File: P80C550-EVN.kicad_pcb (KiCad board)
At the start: 4 copper layers, 98 x 68.8 mm, 78 parts, among them J1 VIN, J10 Analog: +5V, J11 Analog: GND, J2 Signals, J3 Address Low, J4 Address High, J5 LCD, J6 UART, J7 UART, J8 I2C, J9 Analog: In, Q1 Si2393DS, SW1 Reset, U1 P80C550EBAA, U10 MAX691xWE, U11 AP62150WU, U12 74VHC1G02, U13 74VHC1G02, U14 74VHC1G02, U15 74LVC1G373, U16 74VHC1G126, U17 74LVC1G07, U18 74LVC1G06, U2 74AC573, U3 HM62256BLP, U4 28C256, U5 MC146818, U6 AM85C30, U7 74AHC138, U8 PCF8584, U9 74AC00, X1 11.0592 MHz, X2 32.768 KHz

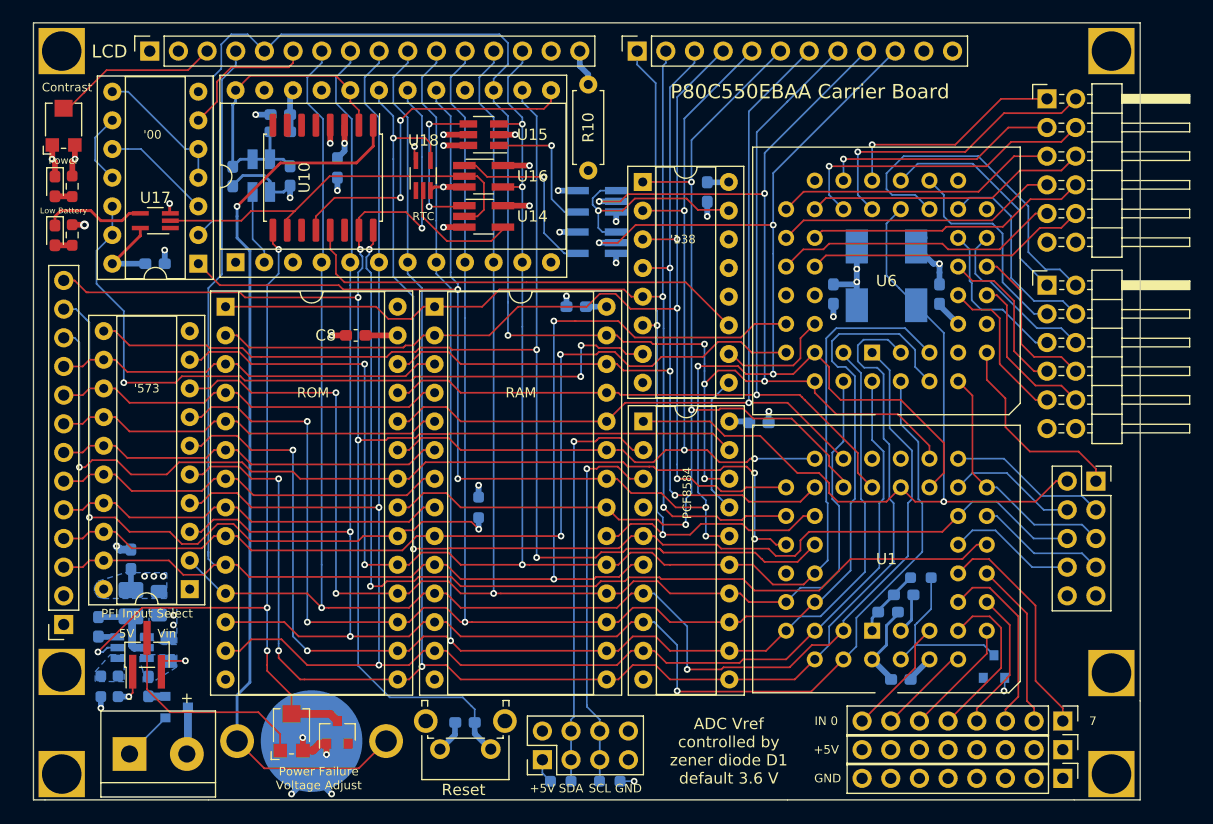
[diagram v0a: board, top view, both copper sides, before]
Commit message: update to KiCAD 6.x and fix the non-inverted reset signal by adding a P-Channel MOSFET to invert the inverted reset signal
Fixes #1 and #2.
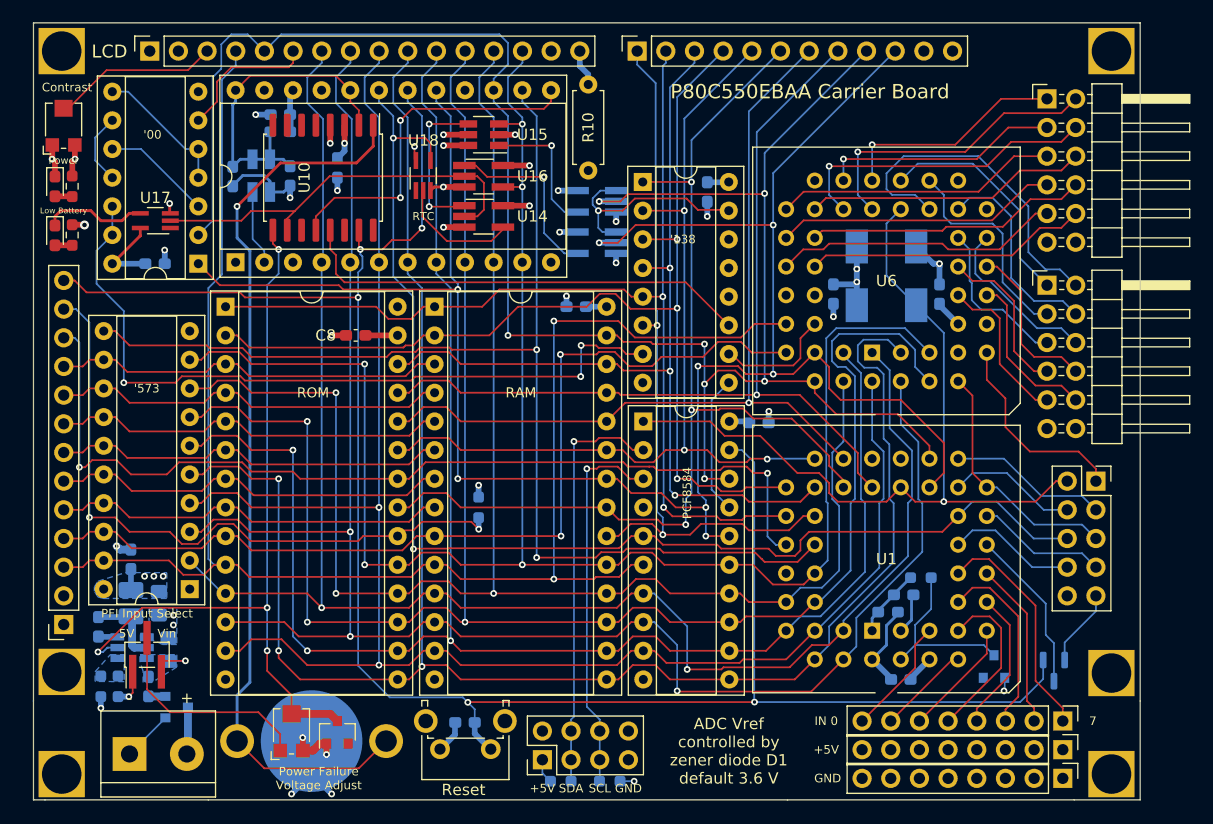
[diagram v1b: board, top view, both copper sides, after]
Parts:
- added Q2: BSS84, Package_TO_SOT_SMD:SOT-23, B.Cu at (188.8, 130.7)
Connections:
- net /~CTSA renamed /~{CTSA}
- net /~CTSB renamed /~{CTSB}
- net /~DCDA renamed /~{DCDA}
- net /~DCDB renamed /~{DCDB}
- net /~DTRA renamed /~{DTRA}
- net /~DTRB renamed /~{DTRB}
- net /~REQA renamed /~{REQA}
- net /~REQB renamed /~{REQB}
- net /~RTSA renamed /~{RTSA}
- net /~RTSB renamed /~{RTSB}
- net /~RTxCA renamed /~{RTxCA}
- net /~RTxCB renamed /~{RTxCB}
- net /~SYNCA renamed /~{SYNCA}
- net /~SYNCB renamed /~{SYNCB}
- net /~TRxCA renamed /~{TRxCA}
- net /~TRxCB renamed /~{TRxCB}
- net ~CODE_CS renamed ~{CODE_CS}
- net ~CODE_RD renamed ~{CODE_RD}
- net ~I2C_CS renamed ~{I2C_CS}
- net ~INT0 renamed ~{INT0}
- net ~INT1 renamed ~{INT1}
- net ~LCD_CS renamed ~{LCD_CS}
- net ~PFO renamed ~{PFO}
- net ~PFO_CS renamed ~{PFO_CS}
- net ~RD renamed ~{RD}
- net ~RST renamed ~{RST}
- net ~RTC_CS renamed ~{RTC_CS}
- net ~RTC_CS_OUT renamed ~{RTC_CS_OUT}
- net ~SCC1_CS renamed ~{SCC1_CS}
- net ~WR renamed ~{WR}
- U1 pad 22: Net-(U1-Pad22) -> unconnected-(U1-Pad22)
- U10 pad 11: Net-(U10-Pad11) -> unconnected-(U10-Pad11)
- U10 pad 14: Net-(U10-Pad14) -> unconnected-(U10-Pad14)
- U10 pad 16: RST -> unconnected-(U10-Pad16)
- U10 pad 5: Net-(U10-Pad5) -> unconnected-(U10-Pad5)
- U10 pad 6: Net-(U10-Pad6) -> unconnected-(U10-Pad6)
- U10 pad 7: Net-(U10-Pad7) -> unconnected-(U10-Pad7)
- U10 pad 8: Net-(U10-Pad8) -> unconnected-(U10-Pad8)
- U5 pad 21: Net-(U5-Pad21) -> unconnected-(U5-Pad21)
- U5 pad 23: Net-(U5-Pad23) -> unconnected-(U5-Pad23)
- U5 pad 3: Net-(U5-Pad3) -> unconnected-(U5-Pad3)
- U7 pad 12: Net-(U7-Pad12) -> unconnected-(U7-Pad12)
- U7 pad 13: Net-(U7-Pad13) -> unconnected-(U7-Pad13)
- U7 pad 14: Net-(U7-Pad14) -> unconnected-(U7-Pad14)
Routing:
- net RST: track 89.8 -> 14.6 mm, vias 2 -> 0
- net ~{RST}: track 135.7 -> 178.1 mm, vias 4 -> 5
- net GND: track 70.1 -> 64.8 mm
- net +5V: track 61.1 -> 66.2 mm
- net /Raw: track 5.23 -> 4.06 mm
- net CLK: track 72.5 -> 71.4 mm
- net /D0: track 147.4 -> 146.3 mm
- net /D5: track 166.8 -> 165.7 mm
- net +15V: track 4.59 -> 3.56 mm
- net /D4: track 157.4 -> 156.5 mm
- net Net-(C16-Pad2): track 4.17 -> 3.38 mm
- net ~{CODE_CS}: track 58.9 -> 58.2 mm
- net /D1: track 159.8 -> 159.2 mm
- net /ADC1: track 8.23 -> 7.72 mm
- net ~{CODE_RD}: track 84.4 -> 84.2 mm, vias 3 -> 2
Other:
- net class Default removed
- board text added: "R/~{W}"
- board text added: "~{CS}"
- board text added: "~{CTS}"
- board text added: "~{DCD}"
- board text added: "~{DTR}"
- board text added: "~{INT0}"
- board text added: "~{INT1}"
- board text added: "~{RD}"
- board text added: "~{REQ}"
- board text added: "~{RST}"
- board text added: "~{RTS}"
- board text added: "~{RTxC}"
- board text added: "~{SYNC}"
- board text added: "~{TRxC}"
- board text added: "~{WR}"
- board text removed: "R/~W"
- board text removed: "~CS"
- board text removed: "~CTS"
- board text removed: "~DCD"
- board text removed: "~DTR"
- board text removed: "~INT0"
- board text removed: "~INT1"
- board text removed: "~RD"
- board text removed: "~REQ"
- board text removed: "~RST"
- board text removed: "~RTS"
- board text removed: "~RTxC"
- board text removed: "~SYNC"
- board text removed: "~TRxC"
- board text removed: "~WR"
